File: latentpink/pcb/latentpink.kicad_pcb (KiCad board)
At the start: 8 copper layers, 145 x 139 mm, 799 parts, among them J1 CONN_SFP_HOST, J10 XILINX_JTAG, J11 FAN_01, J12 FAN_01, J13 CONN_01X05, J14 CONN_01X03, J15 CONN_01X03, J16 JUMPER_0402_SPDT, J17 JUMPER_0402_SPDT, J18 BEL_FUSE_0845-2R1T-E4, J19 BEL_FUSE_0845-2R1T-E4, J2 SFP_CAGE, J20 BEL_FUSE_0845-2R1T-E4, J21 BEL_FUSE_0845-2R1T-E4, J22 BEL_FUSE_0845-2R1T-E4, J23 PMOD_HOST, J3 XILINX_JTAG, J4 BEL_FUSE_0845-2R1T-E4, J5 0826-1G1T-23-F, J6 BARREL_JACK, J7 RJ45, J8 BEL_FUSE_0845-2R1T-E4, J9 XILINX_JTAG, M1 960-27-12-D-AB-0, M10 WEEE, M2 960-23-23-F-AB-0, M3 SCREWHOLE, M4 SCREWHOLE, M5 SCREWHOLE, M6 SCREWHOLE, M7 LONGTHING, M8 OSHW, M9 POLARITY, U1 VSC8512, U10 MYMGK1R812ERSR, U11 MYMGK00504ERSR, U12 STM32L031-QFN32, U13 MYMGK00504ERSR, U14 MYMGK00504ERSR, U15 MYMGK00504ERSR, U16 NCP45521IMNTWG-H, U17 NCP45521IMNTWG-H, U18 LP2996AMRE, U19 TPS7A2533DRVR, U2 XC7K160T-2FBG484C, U20 AT24MAC402, U21 ECX2-LMV-3CN-125.000-TR, U22 ECS-2016MVQ-250-CN, U23 ADM3101E_QFN, U24 SIT9121AI-2BF-XXS200.000000G, U25 SIT9121AI-2BF-XXS156.250000G, U26 74LVC1T45, U27 74LVC1T45, U28 IS25WP256D-JLLE, U29 DSC1123CI2-150.0000T, U3 CY7C2245KV18-450BZXI, U30 DSC1123CI2-150.0000T, U31 74LVC1T45, U32 74LVC1T45, U33 74LVC1T45, U34 74LVC1T45, U35 SIT9121AC-2B2-33E125.000000, U36 AT30TS74_UDFN, U37 AT30TS74_UDFN, U38 AT30TS74_UDFN, U39 AT30TS74_UDFN, U4 STM32H735-UFBGA176-25, U5 DP83867, U6 DP83867, U7 ECS-1612MV-250-CN-TR, U8 ECS-1612MV-250-CN-TR, U9 KSZ9031RN

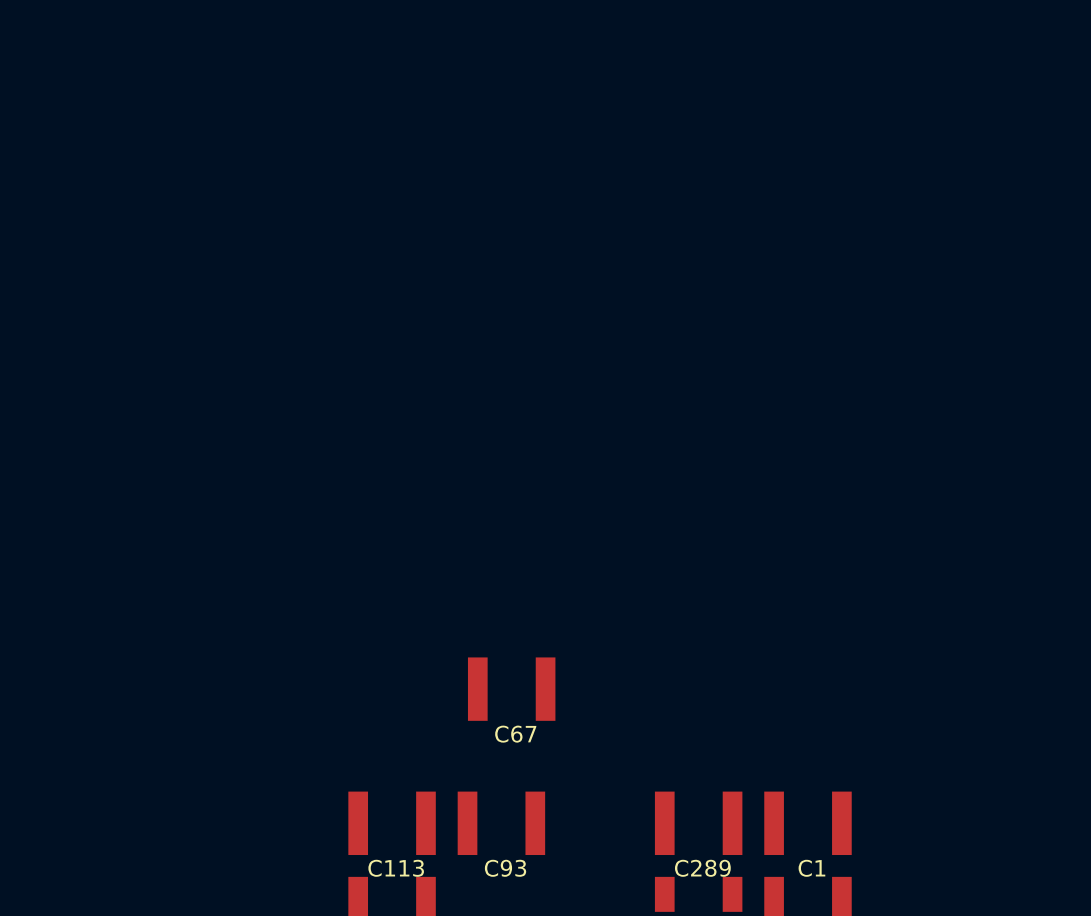
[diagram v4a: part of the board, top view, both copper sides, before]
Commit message: Finished initial schematic review, added ESD diodes to Ethernet pairs
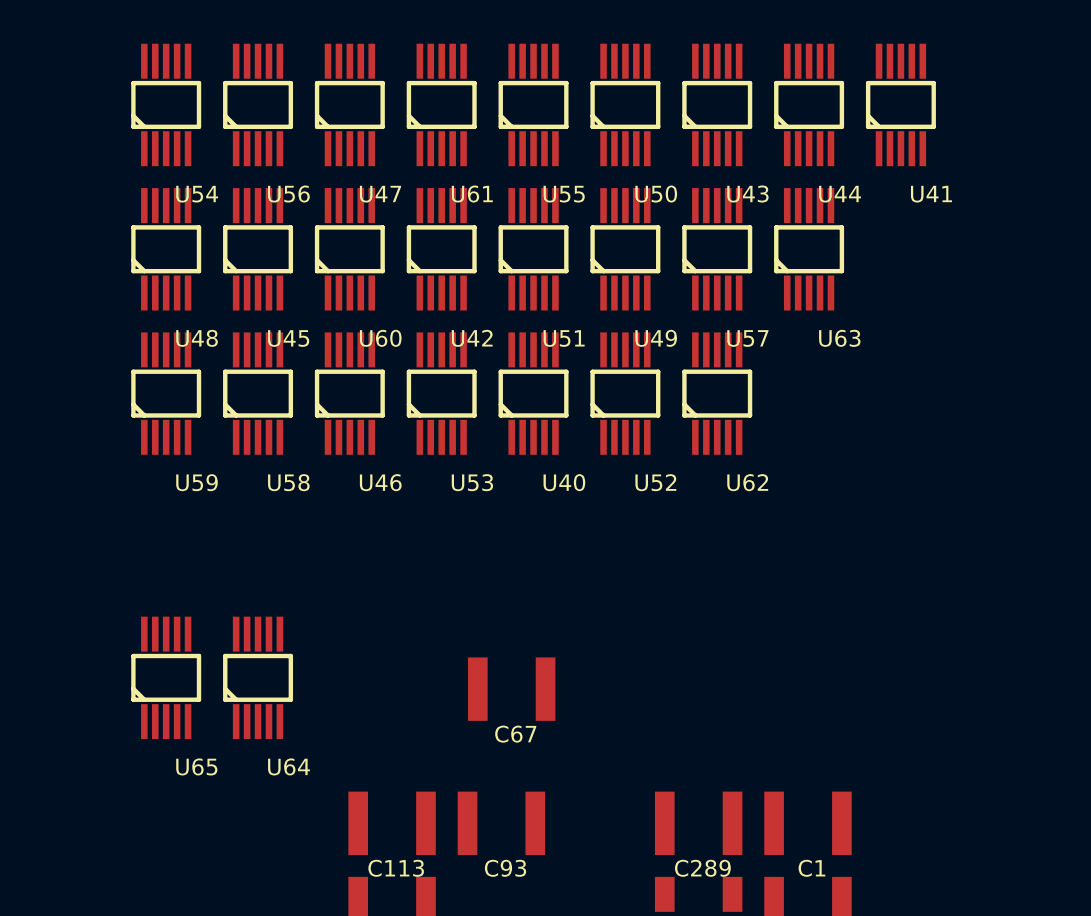
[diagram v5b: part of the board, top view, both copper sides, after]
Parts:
- added U40: RCLAMP0514M, azonenberg_pcb:SOP_10_0.5MM_3MM, F.Cu at (241.0, 16.5)
- added U41: RCLAMP0514M, azonenberg_pcb:SOP_10_0.5MM_3MM, F.Cu at (257.8, 3.30)
- added U42: RCLAMP0514M, azonenberg_pcb:SOP_10_0.5MM_3MM, F.Cu at (236.8, 9.90)
- added U43: RCLAMP0514M, azonenberg_pcb:SOP_10_0.5MM_3MM, F.Cu at (249.4, 3.30)
- added U44: RCLAMP0514M, azonenberg_pcb:SOP_10_0.5MM_3MM, F.Cu at (253.6, 3.30)
- added U45: RCLAMP0514M, azonenberg_pcb:SOP_10_0.5MM_3MM, F.Cu at (228.4, 9.90)
- added U46: RCLAMP0514M, azonenberg_pcb:SOP_10_0.5MM_3MM, F.Cu at (232.6, 16.5)
- added U47: RCLAMP0514M, azonenberg_pcb:SOP_10_0.5MM_3MM, F.Cu at (232.6, 3.30)
- added U48: RCLAMP0514M, azonenberg_pcb:SOP_10_0.5MM_3MM, F.Cu at (224.2, 9.90)
- added U49: RCLAMP0514M, azonenberg_pcb:SOP_10_0.5MM_3MM, F.Cu at (245.2, 9.90)
- added U50: RCLAMP0514M, azonenberg_pcb:SOP_10_0.5MM_3MM, F.Cu at (245.2, 3.30)
- added U51: RCLAMP0514M, azonenberg_pcb:SOP_10_0.5MM_3MM, F.Cu at (241.0, 9.90)
- added U52: RCLAMP0514M, azonenberg_pcb:SOP_10_0.5MM_3MM, F.Cu at (245.2, 16.5)
- added U53: RCLAMP0514M, azonenberg_pcb:SOP_10_0.5MM_3MM, F.Cu at (236.8, 16.5)
- added U54: RCLAMP0514M, azonenberg_pcb:SOP_10_0.5MM_3MM, F.Cu at (224.2, 3.30)
- added U55: RCLAMP0514M, azonenberg_pcb:SOP_10_0.5MM_3MM, F.Cu at (241.0, 3.30)
- added U56: RCLAMP0514M, azonenberg_pcb:SOP_10_0.5MM_3MM, F.Cu at (228.4, 3.30)
- added U57: RCLAMP0514M, azonenberg_pcb:SOP_10_0.5MM_3MM, F.Cu at (249.4, 9.90)
- added U58: RCLAMP0514M, azonenberg_pcb:SOP_10_0.5MM_3MM, F.Cu at (228.4, 16.5)
- added U59: RCLAMP0514M, azonenberg_pcb:SOP_10_0.5MM_3MM, F.Cu at (224.2, 16.5)
- added U60: RCLAMP0514M, azonenberg_pcb:SOP_10_0.5MM_3MM, F.Cu at (232.6, 9.90)
- added U61: RCLAMP0514M, azonenberg_pcb:SOP_10_0.5MM_3MM, F.Cu at (236.8, 3.30)
- added U62: RCLAMP0514M, azonenberg_pcb:SOP_10_0.5MM_3MM, F.Cu at (249.4, 16.5)
- added U63: RCLAMP0514M, azonenberg_pcb:SOP_10_0.5MM_3MM, F.Cu at (253.6, 9.90)
- added U64: RCLAMP0514M, azonenberg_pcb:SOP_10_0.5MM_3MM, F.Cu at (228.4, 29.5)
- added U65: RCLAMP0514M, azonenberg_pcb:SOP_10_0.5MM_3MM, F.Cu at (224.2, 29.5)
- R14: value 10K -> DNP
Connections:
- U12 pad 10: /Power Supply/3V3_PGOOD -> /Power Supply/1V8_EN
- U12 pad 11: /Power Supply/3V3_EN -> /Power Supply/1V2_EN
- U12 pad 12: /Power Supply/2V5_EN -> /Power Supply/1V0_PGOOD
- U12 pad 13: /Power Supply/1V8_EN -> /Power Supply/1V8_PGOOD
- U12 pad 18: /Power Supply/1V2_EN -> /Power Supply/3V3_PGOOD
- U12 pad 19: /Power Supply/1V0_EN -> /Power Supply/1V2_PGOOD
- U12 pad 20: /Power Supply/PWR_OK -> /Power Supply/2V5_PGOOD
- U12 pad 6: /Power Supply/1V0_PGOOD -> /Power Supply/3V3_EN
- U12 pad 7: /Power Supply/1V2_PGOOD -> /Power Supply/PWR_OK
- U12 pad 8: /Power Supply/1V8_PGOOD -> /Power Supply/2V5_EN
- U12 pad 9: /Power Supply/2V5_PGOOD -> /Power Supply/1V0_EN
- U4 pad A2: unconnected-(U4-PadA2) -> /Management/I2C_SCL
- U4 pad B3: unconnected-(U4-PadB3) -> /Management/I2C_SDA

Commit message: Preliminary routing of first four baseT interfaces on VSC8512
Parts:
- U40, U41, U42, U43, U44, U45, U46, U47, U48, U49, U50, U51, U52, U53, U54, U55, U56, U57, U58, U59, U60, U61, U62, U63: moved to B.Cu
- moved TP32 282.0 mm to (-8.93, 137.2)
- moved TP33 282.0 mm to (-14.6, 137.2)
- moved TP34 282.0 mm to (-14.6, 141.6)
- moved TP35 282.0 mm to (-8.93, 141.6)
- moved C1 262.1 mm to (-8.46, 30.5)
- moved C100 262.1 mm to (-28.3, 66.5)
- moved C101 262.1 mm to (-14.4, 50.5)
- moved C102 262.1 mm to (-28.3, 50.5)
- moved C103 262.1 mm to (-21.4, 50.5)
- moved C104 262.1 mm to (-28.3, 54.5)
- moved C105 262.1 mm to (-28.3, 62.5)
- moved C106 262.1 mm to (-56.7, 127.2)
- moved C107 262.1 mm to (-29.4, 38.3)
- moved C108 262.1 mm to (-17.3, 66.3)
- moved C109 262.1 mm to (-15.4, 58.5)
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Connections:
- M3 pad 1: /GND -> /CHGND
- M4 pad 1: /GND -> /CHGND
- M5 pad 1: /GND -> /CHGND
- M6 pad 1: /GND -> /CHGND
- U1 pad A22: /QSGMII PHY/ETH3_D0_P -> /QSGMII PHY/ETH2_D0_P
- U1 pad A23: /QSGMII PHY/ETH3_D1_P -> /QSGMII PHY/ETH2_D1_P
- U1 pad A24: /QSGMII PHY/ETH3_D2_P -> /QSGMII PHY/ETH2_D2_P
- U1 pad A25: /QSGMII PHY/ETH3_D3_P -> /QSGMII PHY/ETH2_D3_P
- U1 pad B22: /QSGMII PHY/ETH3_D0_N -> /QSGMII PHY/ETH2_D0_N
- U1 pad B23: /QSGMII PHY/ETH3_D1_N -> /QSGMII PHY/ETH2_D1_N
- U1 pad B24: /QSGMII PHY/ETH3_D2_N -> /QSGMII PHY/ETH2_D2_N
- U1 pad B25: /QSGMII PHY/ETH3_D3_N -> /QSGMII PHY/ETH2_D3_N
- U1 pad C25: /QSGMII PHY/ETH2_D0_N -> /QSGMII PHY/ETH3_D1_N
- U1 pad C26: /QSGMII PHY/ETH2_D0_P -> /QSGMII PHY/ETH3_D1_P
- U1 pad D25: /QSGMII PHY/ETH2_D1_N -> /QSGMII PHY/ETH3_D0_N
- U1 pad D26: /QSGMII PHY/ETH2_D1_P -> /QSGMII PHY/ETH3_D0_P
- U1 pad E25: /QSGMII PHY/ETH2_D2_N -> /QSGMII PHY/ETH3_D3_N
- U1 pad E26: /QSGMII PHY/ETH2_D2_P -> /QSGMII PHY/ETH3_D3_P
- U1 pad F25: /QSGMII PHY/ETH2_D3_N -> /QSGMII PHY/ETH3_D2_N
- U1 pad F26: /QSGMII PHY/ETH2_D3_P -> /QSGMII PHY/ETH3_D2_P
- U1 pad G25: /QSGMII PHY/ETH1_D0_N -> /QSGMII PHY/ETH0_D0_N
- U1 pad G26: /QSGMII PHY/ETH1_D0_P -> /QSGMII PHY/ETH0_D0_P
- U1 pad H25: /QSGMII PHY/ETH1_D1_N -> /QSGMII PHY/ETH0_D1_N
- U1 pad H26: /QSGMII PHY/ETH1_D1_P -> /QSGMII PHY/ETH0_D1_P
- U1 pad J25: /QSGMII PHY/ETH1_D2_N -> /QSGMII PHY/ETH0_D2_N
- U1 pad J26: /QSGMII PHY/ETH1_D2_P -> /QSGMII PHY/ETH0_D2_P
- U1 pad K25: /QSGMII PHY/ETH1_D3_N -> /QSGMII PHY/ETH0_D3_N
- U1 pad K26: /QSGMII PHY/ETH1_D3_P -> /QSGMII PHY/ETH0_D3_P
- U1 pad L25: /QSGMII PHY/ETH0_D0_N -> /QSGMII PHY/ETH1_D1_N
- U1 pad L26: /QSGMII PHY/ETH0_D0_P -> /QSGMII PHY/ETH1_D1_P
- U1 pad M25: /QSGMII PHY/ETH0_D1_N -> /QSGMII PHY/ETH1_D0_N
- U1 pad M26: /QSGMII PHY/ETH0_D1_P -> /QSGMII PHY/ETH1_D0_P
- U1 pad N25: /QSGMII PHY/ETH0_D2_N -> /QSGMII PHY/ETH1_D3_N
- U1 pad N26: /QSGMII PHY/ETH0_D2_P -> /QSGMII PHY/ETH1_D3_P
- U1 pad P25: /QSGMII PHY/ETH0_D3_N -> /QSGMII PHY/ETH1_D2_N
- U1 pad P26: /QSGMII PHY/ETH0_D3_P -> /QSGMII PHY/ETH1_D2_P
- U48 pad 1: /QSGMII PHY/ETH0_D0_N -> /QSGMII PHY/ETH0_D1_N
- U48 pad 10: /QSGMII PHY/ETH0_D0_N -> /QSGMII PHY/ETH0_D1_N
- U48 pad 2: /QSGMII PHY/ETH0_D0_P -> /QSGMII PHY/ETH0_D1_P
- U48 pad 4: /QSGMII PHY/ETH0_D1_N -> /QSGMII PHY/ETH0_D0_N
- U48 pad 5: /QSGMII PHY/ETH0_D1_P -> /QSGMII PHY/ETH0_D0_P
- U48 pad 6: /QSGMII PHY/ETH0_D1_P -> /QSGMII PHY/ETH0_D0_P
- U48 pad 7: /QSGMII PHY/ETH0_D1_N -> /QSGMII PHY/ETH0_D0_N
- U48 pad 9: /QSGMII PHY/ETH0_D0_P -> /QSGMII PHY/ETH0_D1_P
- U49 pad 1: /QSGMII PHY/ETH0_D2_N -> /QSGMII PHY/ETH0_D3_N
- U49 pad 10: /QSGMII PHY/ETH0_D2_N -> /QSGMII PHY/ETH0_D3_N
- U49 pad 2: /QSGMII PHY/ETH0_D2_P -> /QSGMII PHY/ETH0_D3_P
- U49 pad 4: /QSGMII PHY/ETH0_D3_N -> /QSGMII PHY/ETH0_D2_P
- U49 pad 5: /QSGMII PHY/ETH0_D3_P -> /QSGMII PHY/ETH0_D2_N
- U49 pad 6: /QSGMII PHY/ETH0_D3_P -> /QSGMII PHY/ETH0_D2_N
- U49 pad 7: /QSGMII PHY/ETH0_D3_N -> /QSGMII PHY/ETH0_D2_P
- U49 pad 9: /QSGMII PHY/ETH0_D2_P -> /QSGMII PHY/ETH0_D3_P
- U56 pad 1: /QSGMII PHY/ETH2_D0_N -> /QSGMII PHY/ETH2_D1_N
- U56 pad 10: /QSGMII PHY/ETH2_D0_N -> /QSGMII PHY/ETH2_D1_N
- U56 pad 2: /QSGMII PHY/ETH2_D0_P -> /QSGMII PHY/ETH2_D1_P
- U56 pad 4: /QSGMII PHY/ETH2_D1_N -> /QSGMII PHY/ETH2_D0_N
- U56 pad 5: /QSGMII PHY/ETH2_D1_P -> /QSGMII PHY/ETH2_D0_P
- U56 pad 6: /QSGMII PHY/ETH2_D1_P -> /QSGMII PHY/ETH2_D0_P
- U56 pad 7: /QSGMII PHY/ETH2_D1_N -> /QSGMII PHY/ETH2_D0_N
- U56 pad 9: /QSGMII PHY/ETH2_D0_P -> /QSGMII PHY/ETH2_D1_P
- U57 pad 1: /QSGMII PHY/ETH2_D2_N -> /QSGMII PHY/ETH2_D3_N
- U57 pad 10: /QSGMII PHY/ETH2_D2_N -> /QSGMII PHY/ETH2_D3_N
- U57 pad 2: /QSGMII PHY/ETH2_D2_P -> /QSGMII PHY/ETH2_D3_P
- U57 pad 4: /QSGMII PHY/ETH2_D3_N -> /QSGMII PHY/ETH2_D2_P
- U57 pad 5: /QSGMII PHY/ETH2_D3_P -> /QSGMII PHY/ETH2_D2_N
- U57 pad 6: /QSGMII PHY/ETH2_D3_P -> /QSGMII PHY/ETH2_D2_N
- U57 pad 7: /QSGMII PHY/ETH2_D3_N -> /QSGMII PHY/ETH2_D2_P
- U57 pad 9: /QSGMII PHY/ETH2_D2_P -> /QSGMII PHY/ETH2_D3_P
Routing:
- net /CHGND: track 0.00 -> 308.8 mm
- net /GND: track 0.00 -> 229.6 mm, vias 0 -> 212
- net /3V3: track 0.00 -> 145.7 mm
- net /QSGMII PHY/ETH0_D3_N: track 0.00 -> 81.8 mm, vias 0 -> 2
- net /QSGMII PHY/ETH1_D0_N: track 0.00 -> 80.3 mm, vias 0 -> 2
- net /QSGMII PHY/ETH0_D3_P: track 0.00 -> 80.3 mm, vias 0 -> 2
- net /QSGMII PHY/ETH0_D2_N: track 0.00 -> 78.7 mm, vias 0 -> 2
- net /QSGMII PHY/ETH1_D0_P: track 0.00 -> 78.6 mm, vias 0 -> 2
- net /QSGMII PHY/ETH0_D2_P: track 0.00 -> 77.7 mm, vias 0 -> 2
- net /QSGMII PHY/ETH1_D1_N: track 0.00 -> 77.3 mm, vias 0 -> 2
- net /QSGMII PHY/ETH1_D2_N: track 0.00 -> 77.3 mm, vias 0 -> 2
- net /QSGMII PHY/ETH0_D1_N: track 0.00 -> 76.6 mm, vias 0 -> 2
- net /QSGMII PHY/ETH1_D2_P: track 0.00 -> 75.8 mm, vias 0 -> 2
- net /QSGMII PHY/ETH1_D1_P: track 0.00 -> 75.7 mm, vias 0 -> 2
- net /QSGMII PHY/ETH0_D1_P: track 0.00 -> 75.0 mm, vias 0 -> 2
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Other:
- board text added: "OUTER 140um = 50R 90 um / 90 um = 100R diff (?) INNER 115 um = 50R 81 um / 89 um = 100R diff"
- board text added: "TODO: Simulate via transitions"

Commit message: Continued layout of VSC8512
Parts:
- added TP36: U.FL, azonenberg_pcb:CONN_U.FL_TE_1909763-1, F.Cu at (218.8, 118.2)
- added TP37: U.FL, azonenberg_pcb:CONN_U.FL_TE_1909763-1, F.Cu at (229.5, 125.2)
- added TP38: U.FL, azonenberg_pcb:CONN_U.FL_TE_1909763-1, F.Cu at (214.2, 135.0)
- added TP39: U.FL, azonenberg_pcb:CONN_U.FL_TE_1909763-1, F.Cu at (218.8, 142.0)
- C12, C269, C296, C298, C300, C304, C305, C309, C310, C314, C315, C316, C319, C320, C321, C324, C326, C327, C328, C330, C332, C68, C71, C75, C81, C85, C86, R105, R108: moved to B.Cu
- moved C465 338.0 mm to (245.8, 143.8)
- moved U33 338.0 mm to (249.0, 139.3)
- moved U34 337.5 mm to (249.0, 143.8)
- moved C464 337.4 mm to (245.8, 139.2)
- moved C462 335.8 mm to (245.8, 129.2)
- moved C460 334.8 mm to (242.5, 139.2)
- moved C463 334.1 mm to (245.8, 134.5)
- moved C459 333.9 mm to (242.5, 134.8)
- moved U32 332.8 mm to (249.0, 134.8)
- moved C461 332.6 mm to (242.5, 143.8)
- moved U31 330.5 mm to (249.0, 129.2)
- moved C458 329.8 mm to (242.5, 129.2)
- moved TP19 297.8 mm to (253.8, 109.0)
- moved TP20 297.8 mm to (253.8, 110.5)
- moved C272 291.2 mm to (220.8, 126.3)
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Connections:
- U1 pad A10: /QSGMII PHY/ETH6_D0_P -> /QSGMII PHY/ETH7_D0_P
- U1 pad A11: /QSGMII PHY/ETH6_D1_P -> /QSGMII PHY/ETH7_D1_P
- U1 pad A12: /QSGMII PHY/ETH6_D2_P -> /QSGMII PHY/ETH7_D2_P
- U1 pad A13: /QSGMII PHY/ETH6_D3_P -> /QSGMII PHY/ETH7_D3_P
- U1 pad A14: /QSGMII PHY/ETH5_D0_P -> /QSGMII PHY/ETH4_D0_P
- U1 pad A15: /QSGMII PHY/ETH5_D1_P -> /QSGMII PHY/ETH4_D1_P
- U1 pad A16: /QSGMII PHY/ETH5_D2_P -> /QSGMII PHY/ETH4_D2_P
- U1 pad A17: /QSGMII PHY/ETH5_D3_P -> /QSGMII PHY/ETH4_D3_P
- U1 pad A18: /QSGMII PHY/ETH4_D0_P -> /QSGMII PHY/ETH5_D1_P
- U1 pad A19: /QSGMII PHY/ETH4_D1_P -> /QSGMII PHY/ETH5_D0_P
- U1 pad A20: /QSGMII PHY/ETH4_D2_P -> /QSGMII PHY/ETH5_D3_P
- U1 pad A21: /QSGMII PHY/ETH4_D3_P -> /QSGMII PHY/ETH5_D2_P
- U1 pad A6: /QSGMII PHY/ETH7_D0_P -> /QSGMII PHY/ETH6_D0_P
- U1 pad A7: /QSGMII PHY/ETH7_D1_P -> /QSGMII PHY/ETH6_D1_P
- U1 pad A8: /QSGMII PHY/ETH7_D2_P -> /QSGMII PHY/ETH6_D2_P
- U1 pad A9: /QSGMII PHY/ETH7_D3_P -> /QSGMII PHY/ETH6_D3_P
- U1 pad B10: /QSGMII PHY/ETH6_D0_N -> /QSGMII PHY/ETH7_D0_N
- U1 pad B11: /QSGMII PHY/ETH6_D1_N -> /QSGMII PHY/ETH7_D1_N
- U1 pad B12: /QSGMII PHY/ETH6_D2_N -> /QSGMII PHY/ETH7_D2_N
- U1 pad B13: /QSGMII PHY/ETH6_D3_N -> /QSGMII PHY/ETH7_D3_N
- U1 pad B14: /QSGMII PHY/ETH5_D0_N -> /QSGMII PHY/ETH4_D0_N
- U1 pad B15: /QSGMII PHY/ETH5_D1_N -> /QSGMII PHY/ETH4_D1_N
- U1 pad B16: /QSGMII PHY/ETH5_D2_N -> /QSGMII PHY/ETH4_D2_N
- U1 pad B17: /QSGMII PHY/ETH5_D3_N -> /QSGMII PHY/ETH4_D3_N
- U1 pad B18: /QSGMII PHY/ETH4_D0_N -> /QSGMII PHY/ETH5_D1_N
- U1 pad B19: /QSGMII PHY/ETH4_D1_N -> /QSGMII PHY/ETH5_D0_N
- U1 pad B20: /QSGMII PHY/ETH4_D2_N -> /QSGMII PHY/ETH5_D3_N
- U1 pad B21: /QSGMII PHY/ETH4_D3_N -> /QSGMII PHY/ETH5_D2_N
- U1 pad B6: /QSGMII PHY/ETH7_D0_N -> /QSGMII PHY/ETH6_D0_N
- U1 pad B7: /QSGMII PHY/ETH7_D1_N -> /QSGMII PHY/ETH6_D1_N
- U1 pad B8: /QSGMII PHY/ETH7_D2_N -> /QSGMII PHY/ETH6_D2_N
- U1 pad B9: /QSGMII PHY/ETH7_D3_N -> /QSGMII PHY/ETH6_D3_N
- U41 pad 1: /QSGMII PHY/ETH4_D0_N -> /QSGMII PHY/ETH4_D1_N
- U41 pad 10: /QSGMII PHY/ETH4_D0_N -> /QSGMII PHY/ETH4_D1_N
- U41 pad 2: /QSGMII PHY/ETH4_D0_P -> /QSGMII PHY/ETH4_D1_P
- U41 pad 4: /QSGMII PHY/ETH4_D1_N -> /QSGMII PHY/ETH4_D0_N
- U41 pad 5: /QSGMII PHY/ETH4_D1_P -> /QSGMII PHY/ETH4_D0_P
- U41 pad 6: /QSGMII PHY/ETH4_D1_P -> /QSGMII PHY/ETH4_D0_P
- U41 pad 7: /QSGMII PHY/ETH4_D1_N -> /QSGMII PHY/ETH4_D0_N
- U41 pad 9: /QSGMII PHY/ETH4_D0_P -> /QSGMII PHY/ETH4_D1_P
- U42 pad 1: /QSGMII PHY/ETH4_D2_N -> /QSGMII PHY/ETH4_D3_N
- U42 pad 10: /QSGMII PHY/ETH4_D2_N -> /QSGMII PHY/ETH4_D3_N
- U42 pad 2: /QSGMII PHY/ETH4_D2_P -> /QSGMII PHY/ETH4_D3_P
- U42 pad 4: /QSGMII PHY/ETH4_D3_N -> /QSGMII PHY/ETH4_D2_N
- U42 pad 5: /QSGMII PHY/ETH4_D3_P -> /QSGMII PHY/ETH4_D2_P
- U42 pad 6: /QSGMII PHY/ETH4_D3_P -> /QSGMII PHY/ETH4_D2_P
- U42 pad 7: /QSGMII PHY/ETH4_D3_N -> /QSGMII PHY/ETH4_D2_N
- U42 pad 9: /QSGMII PHY/ETH4_D2_P -> /QSGMII PHY/ETH4_D3_P
- U50 pad 1: /QSGMII PHY/ETH6_D0_N -> /QSGMII PHY/ETH6_D1_N
- U50 pad 10: /QSGMII PHY/ETH6_D0_N -> /QSGMII PHY/ETH6_D1_N
- U50 pad 2: /QSGMII PHY/ETH6_D0_P -> /QSGMII PHY/ETH6_D1_P
- U50 pad 4: /QSGMII PHY/ETH6_D1_N -> /QSGMII PHY/ETH6_D0_N
- U50 pad 5: /QSGMII PHY/ETH6_D1_P -> /QSGMII PHY/ETH6_D0_P
- U50 pad 6: /QSGMII PHY/ETH6_D1_P -> /QSGMII PHY/ETH6_D0_P
- U50 pad 7: /QSGMII PHY/ETH6_D1_N -> /QSGMII PHY/ETH6_D0_N
- U50 pad 9: /QSGMII PHY/ETH6_D0_P -> /QSGMII PHY/ETH6_D1_P
- U51 pad 1: /QSGMII PHY/ETH6_D2_N -> /QSGMII PHY/ETH6_D3_N
- U51 pad 10: /QSGMII PHY/ETH6_D2_N -> /QSGMII PHY/ETH6_D3_N
- U51 pad 2: /QSGMII PHY/ETH6_D2_P -> /QSGMII PHY/ETH6_D3_P
- U51 pad 4: /QSGMII PHY/ETH6_D3_N -> /QSGMII PHY/ETH6_D2_N
- U51 pad 5: /QSGMII PHY/ETH6_D3_P -> /QSGMII PHY/ETH6_D2_P
- U51 pad 6: /QSGMII PHY/ETH6_D3_P -> /QSGMII PHY/ETH6_D2_P
- U51 pad 7: /QSGMII PHY/ETH6_D3_N -> /QSGMII PHY/ETH6_D2_N
- U51 pad 9: /QSGMII PHY/ETH6_D2_P -> /QSGMII PHY/ETH6_D3_P
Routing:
- net /GND: track 229.6 -> 717.2 mm, vias 212 -> 253
- net /3V3: track 145.7 -> 318.6 mm
- net /2V5: track 60.2 -> 162.5 mm, vias 28 -> 37
- net /1V0: track 0.00 -> 88.0 mm, vias 82 -> 81
- net /QSGMII PHY/QSGMII Power/A2V5_VSC: track 0.00 -> 53.7 mm
- net /QSGMII PHY/ETH4_D3_N: track 0.00 -> 48.4 mm, vias 0 -> 2
- net /QSGMII PHY/ETH4_D3_P: track 0.00 -> 48.4 mm, vias 0 -> 2
- net /QSGMII PHY/ETH4_D2_N: track 0.00 -> 47.2 mm, vias 0 -> 2
- net /QSGMII PHY/ETH4_D2_P: track 0.00 -> 47.0 mm, vias 0 -> 2
- net /QSGMII PHY/ETH4_D1_P: track 0.00 -> 46.9 mm, vias 0 -> 2
- net /QSGMII PHY/ETH4_D1_N: track 0.00 -> 46.9 mm, vias 0 -> 2
- net /QSGMII PHY/ETH4_D0_N: track 0.00 -> 45.4 mm, vias 0 -> 2
- net /QSGMII PHY/ETH4_D0_P: track 0.00 -> 45.4 mm, vias 0 -> 2
- net Net-(U1-PadU2): track 0.00 -> 42.0 mm, vias 0 -> 1
- net /QSGMII PHY/ETH5_D0_N: track 0.00 -> 40.2 mm, vias 0 -> 2
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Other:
- board text added: "VSC8512 decoupling"
- board text added: "VSC8512 support"
